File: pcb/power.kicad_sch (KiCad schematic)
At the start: 36 parts, among them J1 USB_C_PowerOnly_6P, U1 AZ1084-3.3, U2 LM66200DRLR

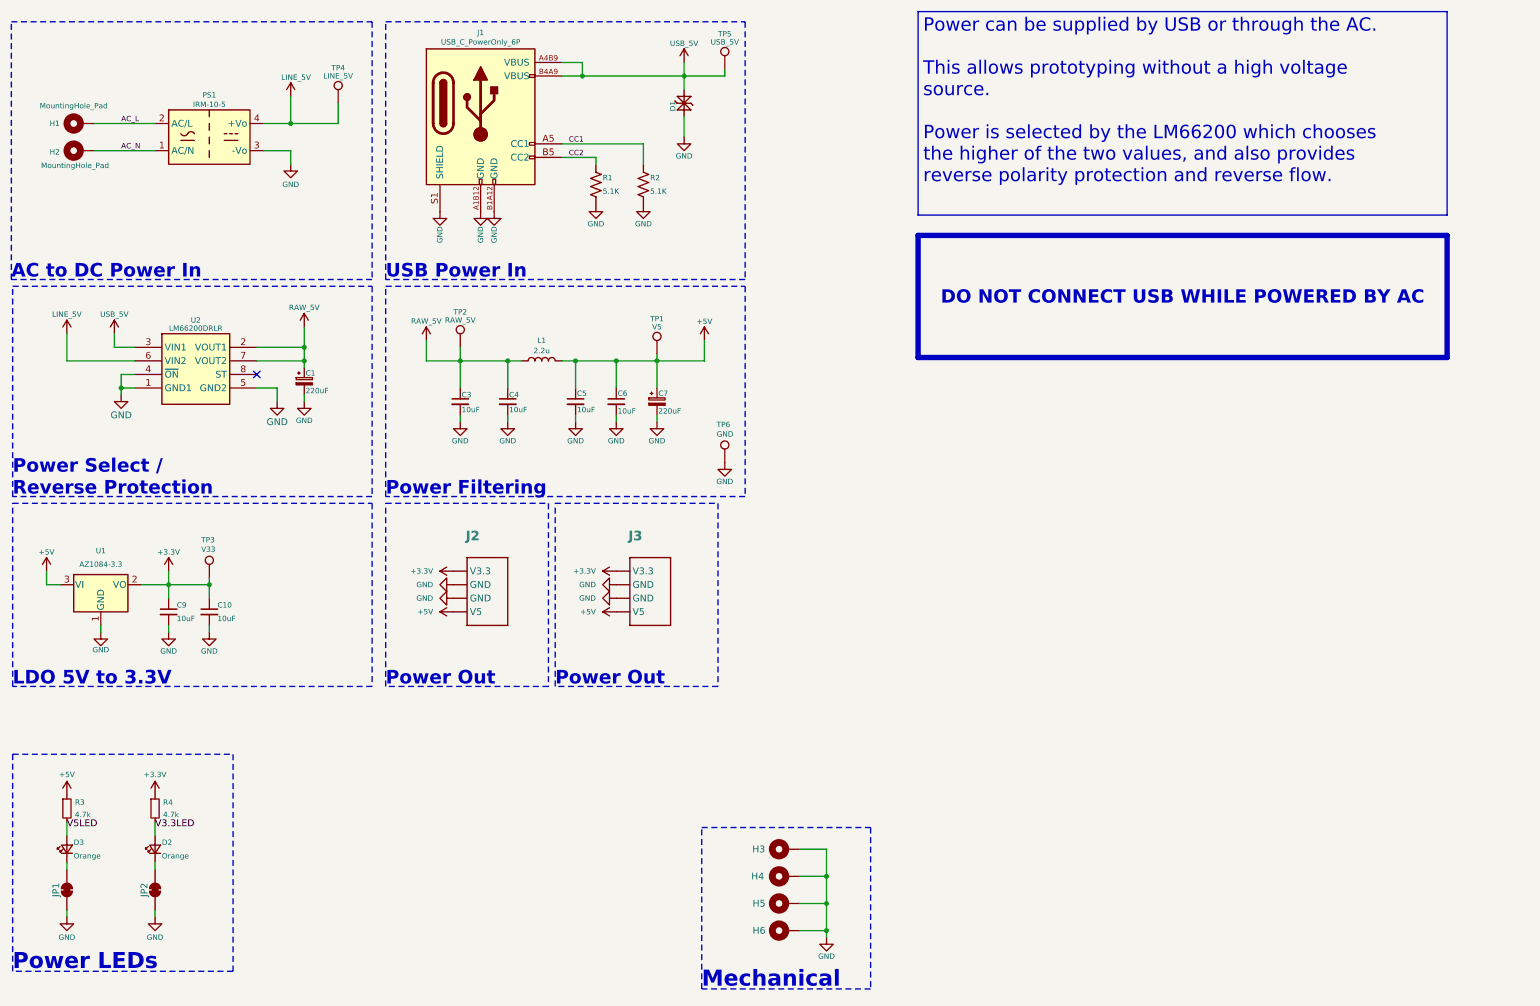
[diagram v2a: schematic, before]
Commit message: Changed power connnectors
Changed to 3 pin power connector for +5v only.
Power input limited to AC or USB only
Added 220uF cap to 3.3v out at LDO
Added TVS to power connectors
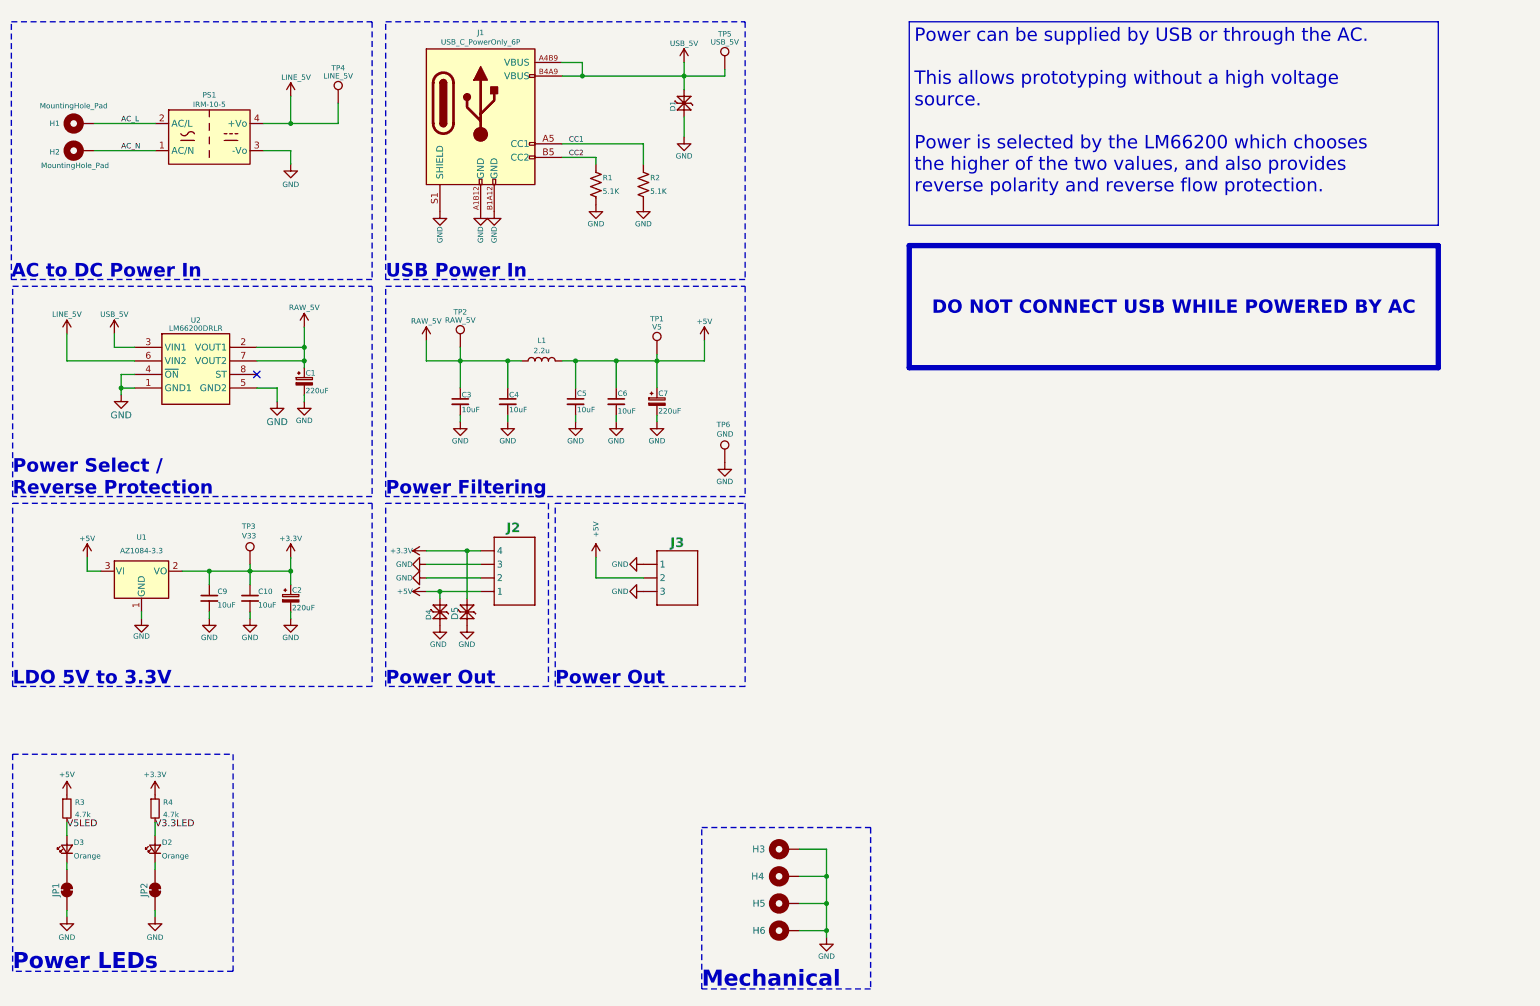
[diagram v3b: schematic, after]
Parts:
- removed J3: ~, CRGM Connector:JST_SH_SM04B-SRSS-TB_1x04-1MP_P1.00mm_Horizontal, symbol CRGM Connector:AQ_POWER
- added C2: 220uF, CRGM Passive:CP_Elec_6.3x5.4, symbol CRGM Passive:C_Polarized_Small
- added D4: PESD5V5C1BL, CRGM Passive:DFN1006-2, symbol CRGM Passive:PESD5V5C1BLYL
- added D5: PESD3V3S1BL, CRGM Passive:DFN1006-2, symbol CRGM Passive:PESD3V3S1BL
- added J3: BM03B-SRSS-TB, CRGM Connector:JST_SH_BM03B-SRSS-TB_1x03-1MP_P1.00mm_Vertical, symbol CRGM Connector:JST-SH-3
- J2: footprint CRGM Connector:JST_SH_SM04B-SRSS-TB_1x04-1MP_P1.00mm_Horizontal -> CRGM Connector:JST_SH_BM04B-SRSS-TB_1x04-1MP_P1.00mm_Vertical; symbol CRGM Connector:AQ_POWER -> CRGM Connector:JST-SH-4; Digikey 455-SM04B-SRSS-TBTR-ND -> 455-BM04B-SRSS-TBTR-ND; MPN SM04B-SRSS-TBT(LF)(SN) -> BM04B-SRSS-TBT(LF)(SN); Mouser 306-SM04BSRSSTBTLFSN -> 306-BM04BSRSSTBTLFSN
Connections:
- net +3.3V: now also C2.1, D5.2 (K2)
- net +5V: now also D4.2 (K2), J3.2
- net GND: now also C2.2, D4.1 (K1), D5.1 (K1), J3.1, J3.3
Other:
- moved on the sheet: C10, C9, J2, TP3, U1
